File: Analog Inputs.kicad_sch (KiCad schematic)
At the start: 28 parts, among them J10 Screw_Terminal_01x06, J8 Screw_Terminal_01x06, J9 Screw_Terminal_01x06, U3 REF35102QDBVR, U4 ADS1256, U5 ADS1256, Y1 8.0Mhz, Y2 8.0Mhz

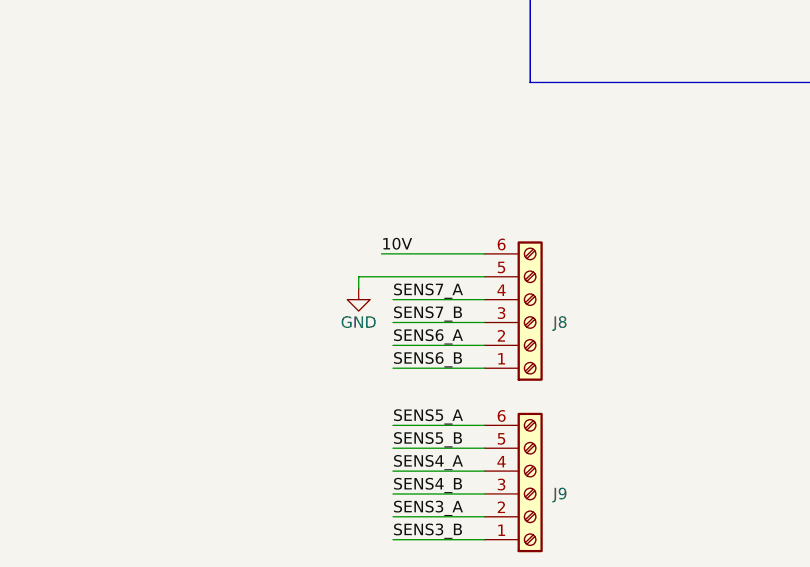
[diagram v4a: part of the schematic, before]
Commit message: Se empieza a evaluar la conexión del ethernet con la carcasa, parte analog, dig y micro en posición, tambien se busca solución para la salida de led de las entradas digitales
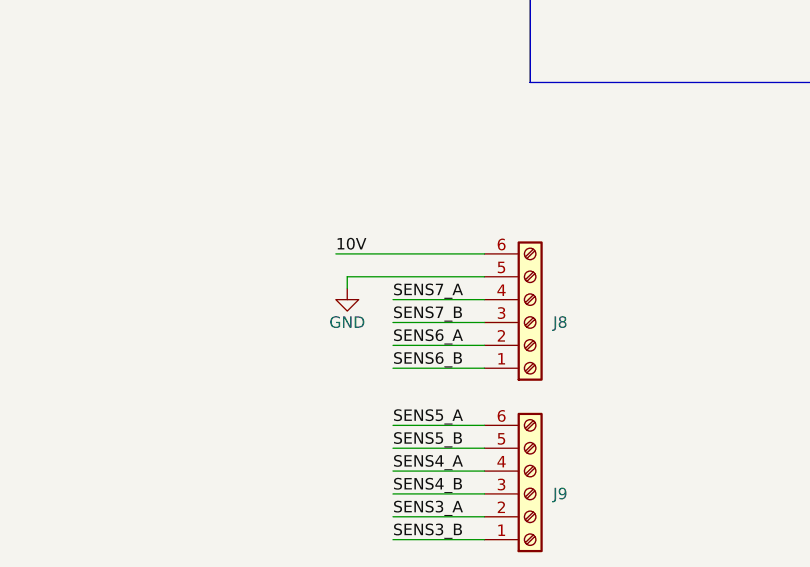
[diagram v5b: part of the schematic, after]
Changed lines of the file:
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@@
 	(wire
 		(pts
-			(xy 326.39 127) (xy 340.36 127)
-		)
-		(stroke
-			(width 0)
-			(type default)
-		)
-	)
-	(wire
-		(pts
 			(xy 160.02 100.33) (xy 167.64 100.33)
 		)
@@
 	(wire
 		(pts
+			(xy 340.36 124.46) (xy 323.85 124.46)
+		)
+		(stroke
+			(width 0)
+			(type default)
+		)
+	)
+	(wire
+		(pts
 			(xy 123.19 87.63) (xy 123.19 85.09)
 		)
@@
 	(wire
 		(pts
+			(xy 325.12 127) (xy 340.36 127)
+		)
+		(stroke
+			(width 0)
+			(type default)
+		)
+	)
+	(wire
+		(pts
 			(xy 43.18 93.98) (xy 31.75 93.98)
 		)
@@
 	(wire
 		(pts
+			(xy 325.12 128.27) (xy 325.12 127)
+		)
+		(stroke
+			(width 0)
+			(type default)
+		)
+	)
+	(wire
+		(pts
 			(xy 173.99 205.74) (xy 173.99 207.01)
 		)
@@
 	(wire
 		(pts
-			(xy 340.36 124.46) (xy 328.93 124.46)
-		)
-		(stroke
-			(width 0)
-			(type default)
-		)
-	)
-	(wire
-		(pts
 			(xy 162.56 193.04) (xy 162.56 175.26)
 		)
@@
 	(wire
 		(pts
-			(xy 326.39 128.27) (xy 326.39 127)
-		)
-		(stroke
-			(width 0)
-			(type default)
-		)
-	)
-	(wire
-		(pts
 			(xy 82.55 215.9) (xy 82.55 217.17)
 		)
@@
 		)
 	)
+	(label "10V"
+		(at 323.85 124.46 0)
+		(effects
+			(font
+				(size 1.27 1.27)
+			)
+			(justify left bottom)
+		)
+	)
 	(label "IN3_N"
 		(at 167.64 218.44 180)
@@
 		)
 	)
-	(label "10V"
-		(at 328.93 124.46 0)
-		(effects
-			(font
-				(size 1.27 1.27)
-			)
-			(justify left bottom)
-		)
-	)
 	(label "IN2_P"
 		(at 250.19 203.2 0)
@@
 	(symbol
 		(lib_id "power:GND")
-		(at 326.39 128.27 0)
+		(at 325.12 128.27 0)
 		(mirror y)
 		(unit 1)
@@
 		(dnp no)
 		(property "Reference" "#PWR0116"
-			(at 326.39 134.62 0)
+			(at 325.12 134.62 0)
 			(effects
 				(font
@@
 		)
 		(property "Value" "GND"
-			(at 326.39 132.08 0)
+			(at 325.12 132.08 0)
 			(effects
 				(font
@@
 		)
 		(property "Footprint" ""
-			(at 326.39 128.27 0)
+			(at 325.12 128.27 0)
 			(effects
 				(font
@@
 		)
 		(property "Datasheet" ""
-			(at 326.39 128.27 0)
+			(at 325.12 128.27 0)
 			(effects
 				(font
@@
 		)
 		(property "Description" "Power symbol creates a global label with name \"GND\" , ground"
-			(at 326.39 128.27 0)
+			(at 325.12 128.27 0)
 			(effects
 				(font

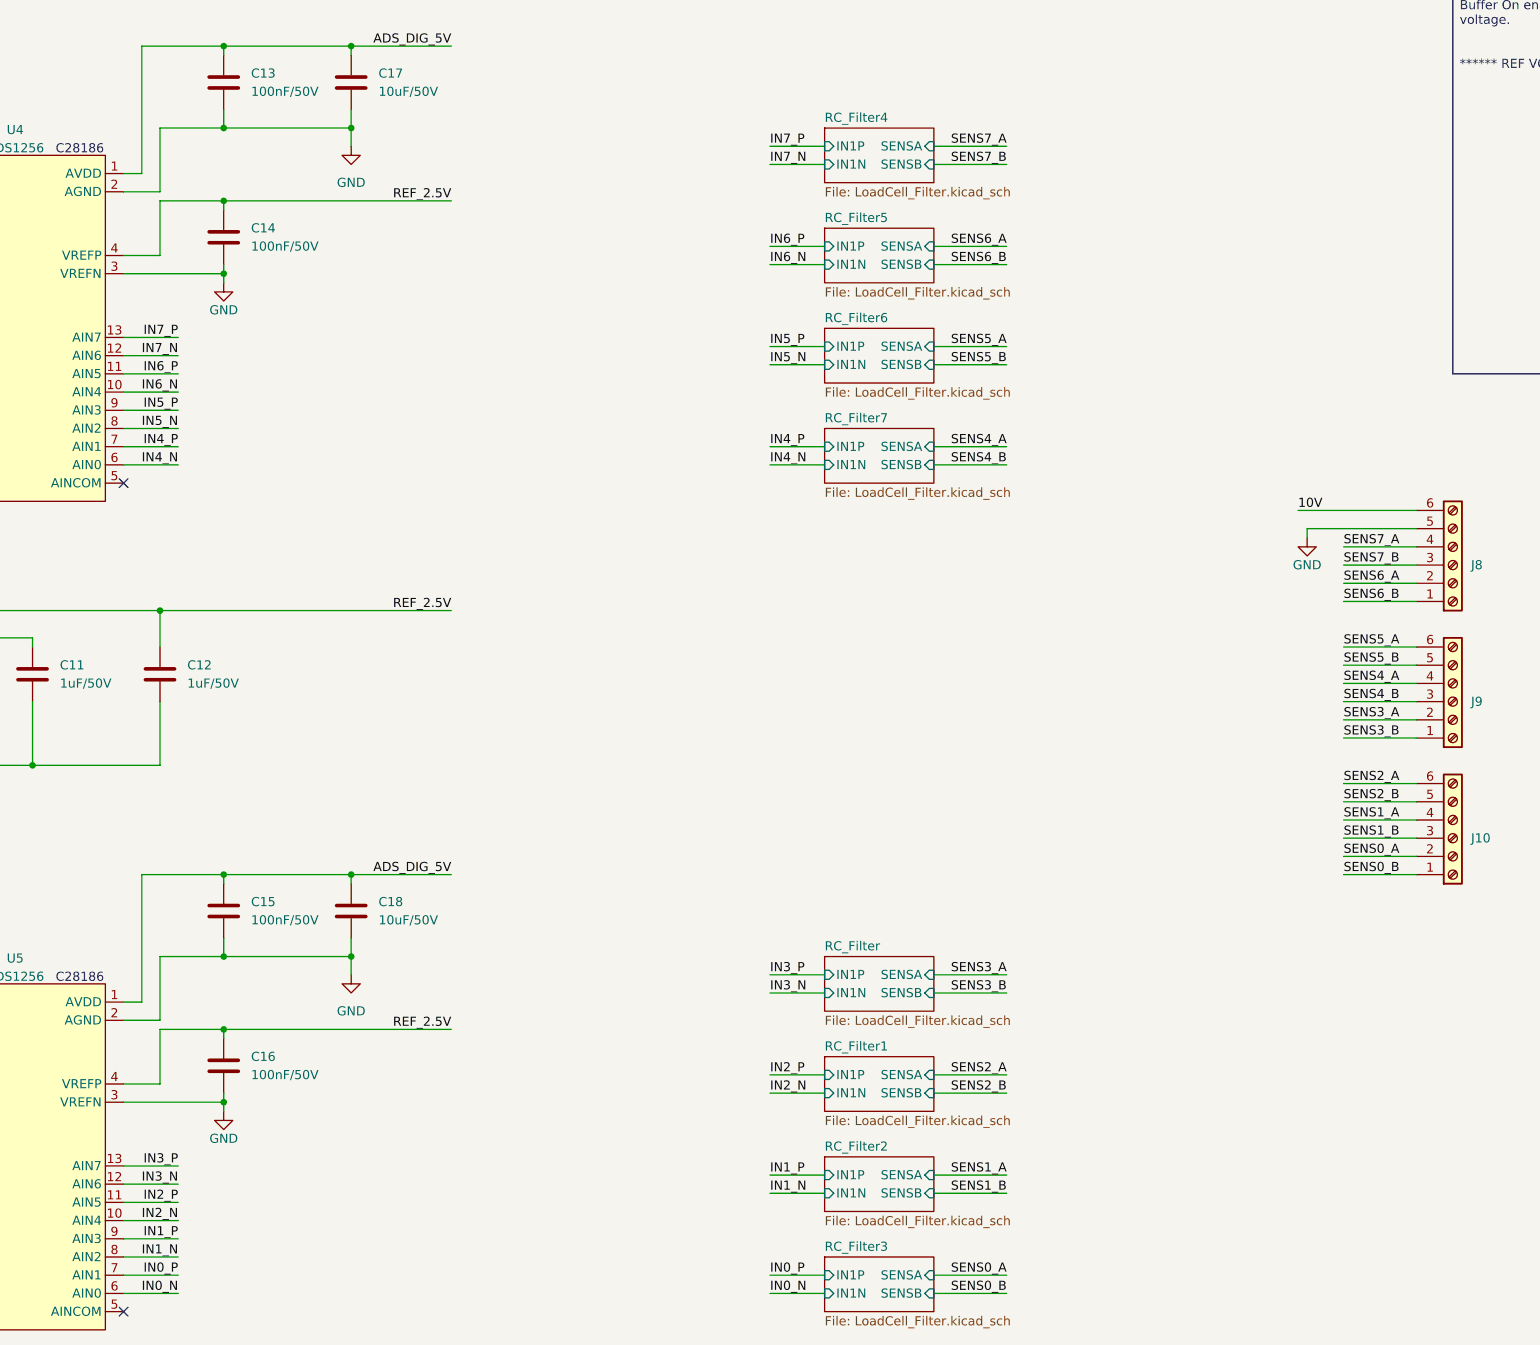
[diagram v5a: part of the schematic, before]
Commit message: Se termina de revisar la placa. Se corrige la terminación de los transformadores internos del puerto ethernet. Se revisa GND, espaciado, añadimos notas. Falta enlazar las partes de JLCPCN
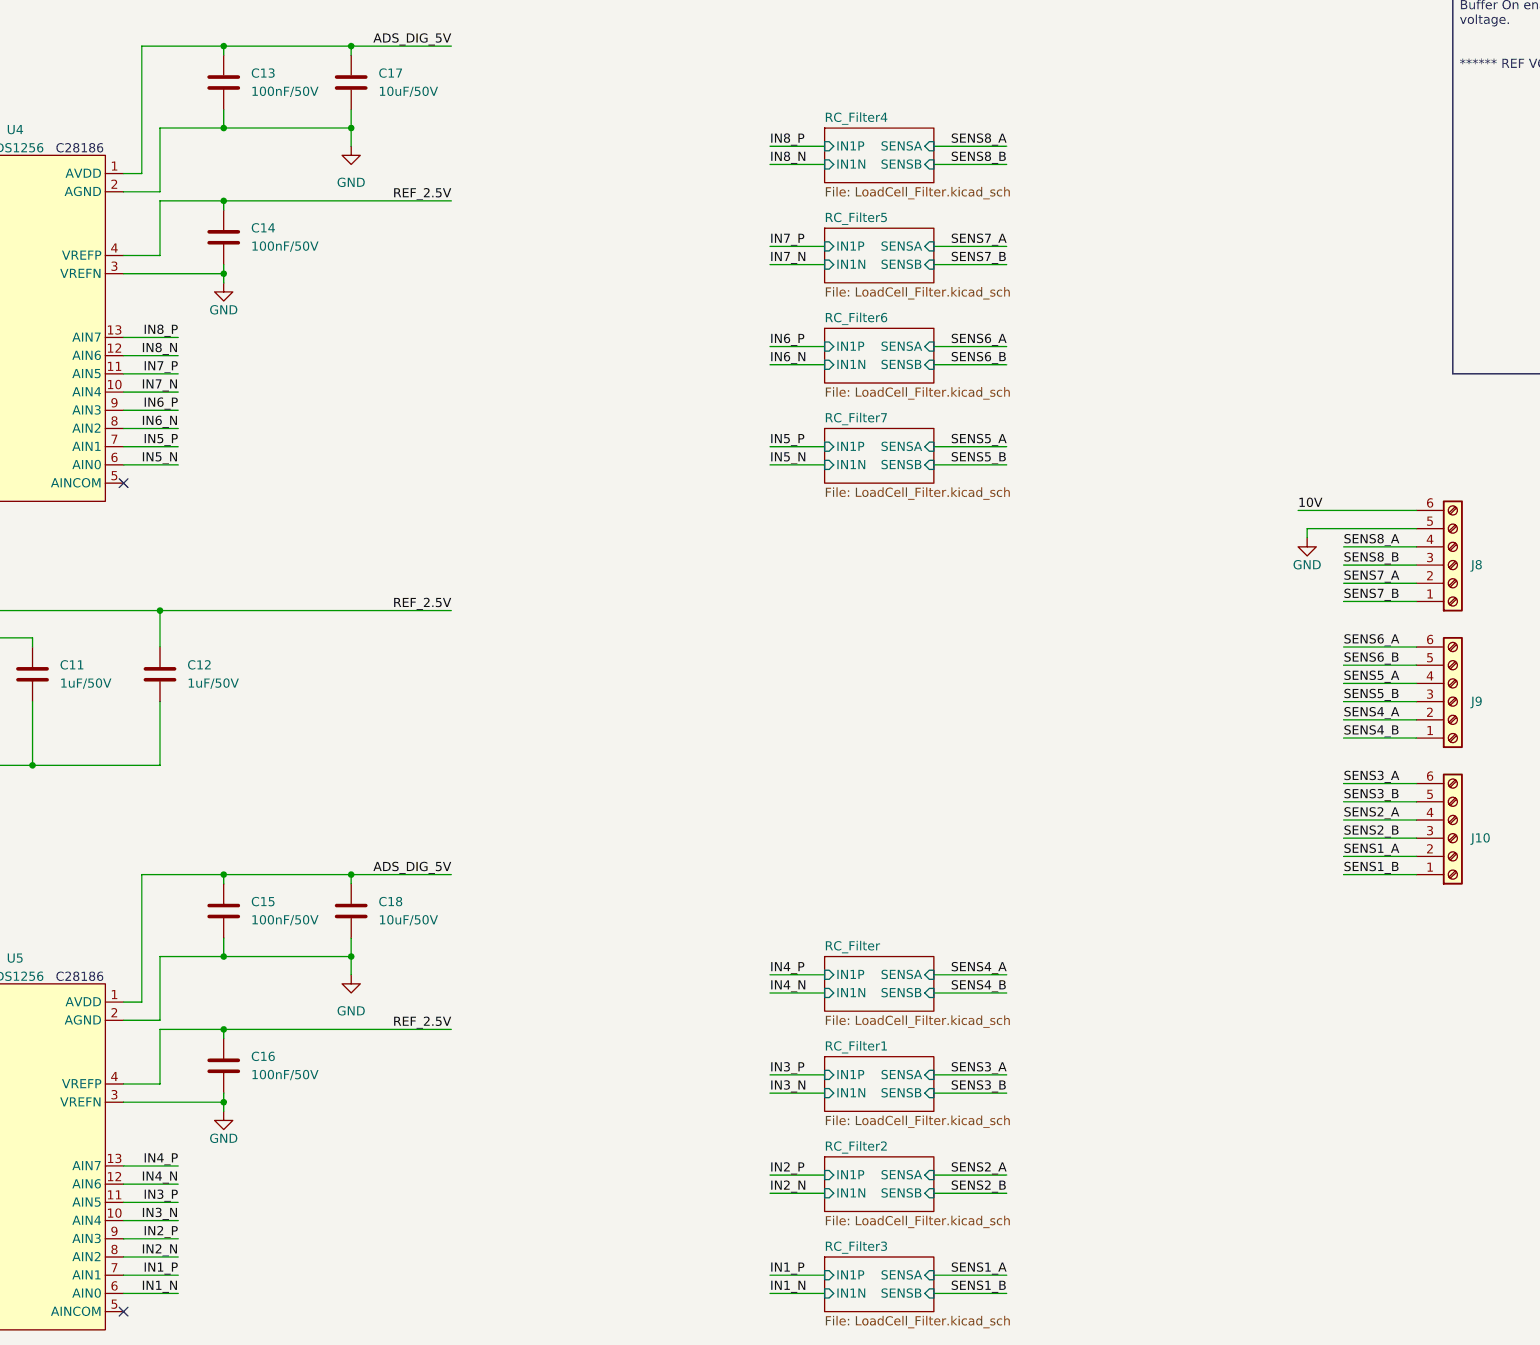
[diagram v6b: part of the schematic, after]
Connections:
- net IN0_N is gone; now on net IN1_N: U5.6 (AIN0)
- net IN0_P is gone; now on net IN1_P: U5.7 (AIN1)
- net SENS0_A is gone; now on net SENS1_A: J10.2 (Pin_2)
- net SENS0_B is gone; now on net SENS1_B: J10.1 (Pin_1)
- net IN1_N: no longer U5.8 (AIN2)
- net IN1_P: no longer U5.9 (AIN3)
- net IN2_N: now also U5.8 (AIN2); no longer U5.10 (AIN4)
- net IN2_P: now also U5.9 (AIN3); no longer U5.11 (AIN5)
- net IN3_N: now also U5.10 (AIN4); no longer U5.12 (AIN6)
- net IN3_P: now also U5.11 (AIN5); no longer U5.13 (AIN7)
- net IN4_N: now also U5.12 (AIN6); no longer U4.6 (AIN0)
- net IN4_P: now also U5.13 (AIN7); no longer U4.7 (AIN1)
- net IN5_N: now also U4.6 (AIN0); no longer U4.8 (AIN2)
- net IN5_P: now also U4.7 (AIN1); no longer U4.9 (AIN3)
- net IN6_N: now also U4.8 (AIN2); no longer U4.10 (AIN4)
- net IN6_P: now also U4.9 (AIN3); no longer U4.11 (AIN5)
- net IN7_N: now also U4.10 (AIN4); no longer U4.12 (AIN6)
- net IN7_P: now also U4.11 (AIN5); no longer U4.13 (AIN7)
- net SENS1_A: no longer J10.4 (Pin_4)
- net SENS1_B: no longer J10.3 (Pin_3)
- net SENS2_A: now also J10.4 (Pin_4); no longer J10.6 (Pin_6)
- net SENS2_B: now also J10.3 (Pin_3); no longer J10.5 (Pin_5)
- net SENS3_A: now also J10.6 (Pin_6); no longer J9.2 (Pin_2)
- net SENS3_B: now also J10.5 (Pin_5); no longer J9.1 (Pin_1)
- net SENS4_A: now also J9.2 (Pin_2); no longer J9.4 (Pin_4)
- net SENS4_B: now also J9.1 (Pin_1); no longer J9.3 (Pin_3)
- net SENS5_A: now also J9.4 (Pin_4); no longer J9.6 (Pin_6)
- net SENS5_B: now also J9.3 (Pin_3); no longer J9.5 (Pin_5)
- net SENS6_A: now also J9.6 (Pin_6); no longer J8.2 (Pin_2)
- net SENS6_B: now also J9.5 (Pin_5); no longer J8.1 (Pin_1)
- net SENS7_A: now also J8.2 (Pin_2); no longer J8.4 (Pin_4)
- net SENS7_B: now also J8.1 (Pin_1); no longer J8.3 (Pin_3)
- new net IN8_N: U4.12 (AIN6)
- new net IN8_P: U4.13 (AIN7)
- new net SENS8_A: J8.4 (Pin_4)
- new net SENS8_B: J8.3 (Pin_3)

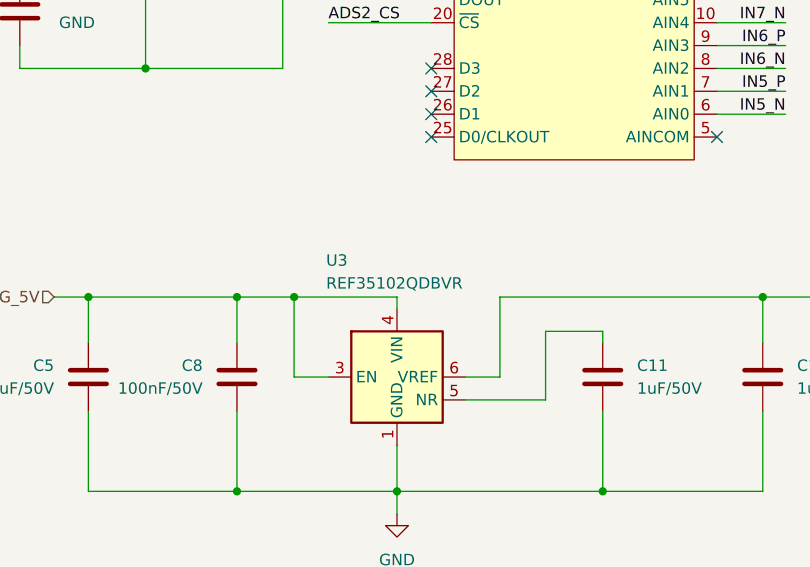
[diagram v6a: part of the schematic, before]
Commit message: Se corrige el nombre para la ref de 2.5V para los canales análogos, Se corrigen quita un capacitor en cada pin VCAP, Se actualiza PCB
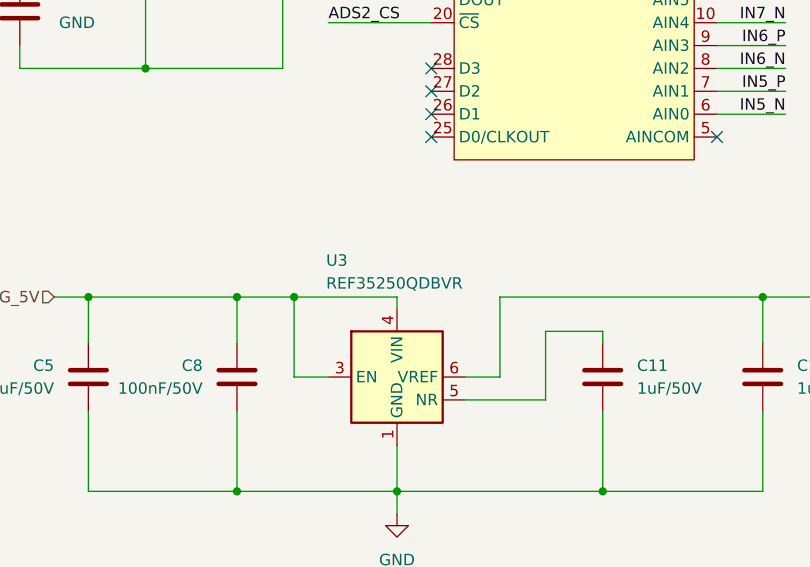
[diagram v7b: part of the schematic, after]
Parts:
- U3: value REF35102QDBVR -> REF35250QDBVR
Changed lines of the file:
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@@
 			)
 		)
-		(property "Value" "REF35102QDBVR"
+		(property "Value" "REF35250QDBVR"
 			(at 116.586 136.906 0)
 			(effects
